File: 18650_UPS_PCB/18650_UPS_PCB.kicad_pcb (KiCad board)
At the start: 4 copper layers, 90 x 62 mm, 68 parts, among them J1 USB_B_Micro, J10 Conn_02x06_Odd_Even, J11 Conn_02x07_Odd_Even, J6 Conn_02x01, J9 Conn_02x04_Odd_Even, SW1 ENABLE, SW2 5_Way_Tactile, SW3 PWR MODE, SW5 ENABLE, U1 STLINK-V3MINI, U10 STLINK-V3MINI, U2 R5478, U3 STC4054, U4 FS8205A, U5 TPS63000, U6 TPS63000, U7 SSD1306_128_32, U8 INA219AxD, U9 STM32F030F4Px

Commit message: first routing done
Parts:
- removed JP3: A0_SEL, Jumper:SolderJumper-3_P1.3mm_Open_RoundedPad1.0x1.5mm
- removed JP4: A1_SEL, Jumper:SolderJumper-3_P1.3mm_Open_RoundedPad1.0x1.5mm
- removed R14, R15: 3.3 kOhm, Resistor_SMD:R_0603_1608Metric
- removed SW2: 5_Way_Tactile, CUSTOM_FOOTPRINTS:5_Way_Tactical
- added SW4: ALPSALPINE_SKRHADE011, CUSTOM_FOOTPRINTS:SKRHADE011, F.Cu at (154.5, 90.1)
- BT1: moved to B.Cu
- U7: footprint Connector_PinSocket_2.54mm:PinSocket_1x04_P2.54mm_Vertical -> Connector_PinHeader_2.54mm:PinHeader_1x04_P2.54mm_Vertical_SMD_Pin1Left
- moved J11 110.2 mm to (194.4, 79.2), turned to 270 degrees
- moved U1 101.3 mm to (177.1, 99.5)
- moved JP5 97.0 mm to (187.7, 100.7), turned to 270 degrees
- moved R12 92.6 mm to (188.1, 97.1), turned to 90 degrees
- moved R13 91.4 mm to (185.9, 97.1), turned to 90 degrees
- moved U7 88.6 mm to (164.5, 89.0)
- moved C10 85.8 mm to (140.9, 78.5)
- moved C8 85.8 mm to (140.9, 76.5)
- moved R10 85.8 mm to (144.5, 78.5)
- moved C9 85.7 mm to (144.5, 76.5)
- moved C13 85.5 mm to (171.7, 85.2)
- moved C6 84.8 mm to (144.7, 92.3)
- moved R8 84.7 mm to (144.5, 81.5), turned to 0 degrees
- moved C18 84.6 mm to (171.7, 88.6)
- moved C19 84.5 mm to (171.7, 90.6)
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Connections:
- U8 pad 1: Net-(JP4-Pad2) -> GNDD
- U8 pad 2: Net-(JP3-Pad2) -> GNDD
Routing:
- net GNDD: track 0.00 -> 127.0 mm, vias 0 -> 11
- net -BATT: track 0.00 -> 124.3 mm, vias 0 -> 11
- net I2C1_SCL: track 0.06 -> 102.2 mm, vias 0 -> 5
- net I2C1_SDA: track 0.00 -> 81.9 mm, vias 0 -> 3
- net RSPI1_MOSI: track 0.00 -> 67.4 mm, vias 0 -> 2
- net RSPI1_SCLK: track 0.00 -> 62.1 mm, vias 0 -> 2
- net RSPI1_MISO: track 0.00 -> 61.8 mm, vias 0 -> 2
- net PB1: track 0.00 -> 56.0 mm, vias 0 -> 2
- net RSPI1_CE2: track 0.00 -> 53.9 mm, vias 0 -> 2
- net PA9: track 0.00 -> 53.6 mm, vias 0 -> 2
- net RSPI0_CE0: track 8.30 -> 51.8 mm, vias 0 -> 2
- net Shunt-: track 0.00 -> 40.9 mm, vias 0 -> 3
- net PA10: track 0.00 -> 39.3 mm, vias 0 -> 2
- net RSPI0_SCLK: track 7.90 -> 43.6 mm, vias 0 -> 2
- net RSPI0_MISO: track 6.71 -> 40.6 mm, vias 0 -> 2
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- added copper zone on B.Cu, net -BATT
- added copper zone on F.Cu, net -BATT
- added copper zone on In2.Cu, net -BATT
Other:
- board size 90 x 62 mm -> 90 x 30 mm

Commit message: layout almost done
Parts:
- removed J10: Conn_02x06_Odd_Even, Connector_PinSocket_2.54mm:PinSocket_2x06_P2.54mm_Vertical_SMD
- removed J11: Conn_02x07_Odd_Even, Connector_PinSocket_2.54mm:PinSocket_2x07_P2.54mm_Vertical_SMD
- removed J6: Conn_02x01, Connector_PinSocket_2.54mm:PinSocket_2x03_P2.54mm_Vertical_SMD
- removed J9: Conn_02x04_Odd_Even, Connector_PinSocket_2.54mm:PinSocket_2x04_P2.54mm_Vertical_SMD
- removed JP1, JP2: PWRSAVE, Jumper:SolderJumper-3_P1.3mm_Open_RoundedPad1.0x1.5mm
- removed JP5: Jumper_NO_Small, Jumper:SolderJumper-2_P1.3mm_Open_RoundedPad1.0x1.5mm
- removed SW3: PWR MODE, Button_Switch_THT:SW_CuK_OS102011MA1QN1_SPDT_Angled
- removed SW4: ALPSALPINE_SKRHADE011, CUSTOM_FOOTPRINTS:SKRHADE011
- removed SW5: ENABLE, Button_Switch_THT:SW_CuK_OS102011MA1QN1_SPDT_Angled
- removed U10: STLINK-V3MINI, Connector_PinHeader_1.27mm:PinHeader_2x07_P1.27mm_Vertical_SMD
- added J2: Conn_02x04_Odd_Even, Connector_PinSocket_2.54mm:PinSocket_2x04_P2.54mm_Vertical_SMD, F.Cu at (156.5, 78.9)
- added SW2: ALPSALPINE_SKRHADE011, CUSTOM_FOOTPRINTS:SKRHADE011, F.Cu at (199.6, 89.7)
- BT1: footprint CUSTOM_FOOTPRINTS:Keystone_1042 -> Battery:BatteryHolder_Keystone_1042_1x18650
- SW1: value ENABLE -> SW_SPDT; footprint Button_Switch_THT:SW_CuK_OS102011MA1QN1_SPDT_Angled -> CUSTOM_FOOTPRINTS:ALPS_SPEF210101
- U7: value SSD1306_128_32 -> INA219AxD; footprint Connector_PinHeader_2.54mm:PinHeader_1x04_P2.54mm_Vertical_SMD_Pin1Left -> Package_SO:SOIC-8_3.9x4.9mm_P1.27mm
- U8: value INA219AxD -> SSD1306_128_32; footprint Package_SO:SOIC-8_3.9x4.9mm_P1.27mm -> Connector_PinHeader_2.54mm:PinHeader_1x04_P2.54mm_Vertical_SMD_Pin1Left
- moved U4 83.6 mm to (206.5, 84.3), turned to 0 degrees
- moved R2 81.9 mm to (126.6, 87.1), turned to 0 degrees
- moved U3 76.5 mm to (125.8, 83.1), turned to 0 degrees
- moved D1 76.1 mm to (129.1, 78.4), turned to 90 degrees
- moved U2 75.3 mm to (201.9, 79.2)
- moved R4 72.6 mm to (198.8, 79.4), turned to 90 degrees
- moved C2 72.3 mm to (198.8, 75.4)
- moved R1 72.1 mm to (202.3, 75.4)
- moved R3 70.6 mm to (132.3, 76.9), turned to 0 degrees
- moved R5 69.3 mm to (132.4, 80.2)
- moved C3 68.9 mm to (131.5, 83.1), turned to 270 degrees
- moved C1 67.0 mm to (133.5, 83.1), turned to 270 degrees
- moved J1 59.5 mm to (145.3, 76.7), turned to 180 degrees
- moved C12 57.4 mm to (137.8, 93.9), turned to 90 degrees
- moved C8 44.2 mm to (185.1, 76.5), turned to 90 degrees
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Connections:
- BT1 pad 1: Shunt+ -> Net-(BT1-Pad1)
- C13 pad 1: GNDD -> +3V3
- C13 pad 2: NRST -> GNDD
- C14 pad 1: +3V3 -> GNDD
- C14 pad 2: GNDD -> NRST
- C15 pad 2: MCU_PWR -> +3V3
- C16 pad 2: MCU_PWR -> +3V3
- C17 pad 2: MCU_PWR -> +3V3
- C18 pad 1: MCU_PWR -> +3V3
- C19 pad 1: MCU_PWR -> +3V3
- R12 pad 1: Net-(JP5-Pad1) -> +3V3
- R13 pad 1: Net-(JP5-Pad1) -> +3V3
- SW1 pad 1: Net-(C6-Pad2) -> Net-(SW1-Pad1)
- SW1 pad 2: Net-(JP1-Pad3) -> Net-(BT1-Pad1)
- SW1 pad 3: GNDD -> Shunt+
- U1 pad 3: MCU_PWR -> +3V3
- U5 pad 6: Net-(JP1-Pad3) -> Net-(C6-Pad2)
- U5 pad 7: Net-(JP1-Pad2) -> PA4
- U6 pad 6: Net-(JP2-Pad3) -> Net-(C7-Pad2)
- U6 pad 7: Net-(JP2-Pad2) -> PA5
- U7 pad 2: MCU_PWR -> GNDD
- U7 pad 3: I2C1_SCL -> I2C1_SDA
- U7 pad 4: I2C1_SDA -> I2C1_SCL
- U8 pad 2: GNDD -> +3V3
- U8 pad 3: I2C1_SDA -> I2C1_SCL
- U8 pad 4: I2C1_SCL -> I2C1_SDA
- U9 pad 10: RSPI0_CE0 -> PA4
- U9 pad 11: RSPI0_SCLK -> PA5
- U9 pad 12: RSPI0_MISO -> Net-(U9-Pad12)
- U9 pad 13: RSPI0_MOSI -> Net-(U9-Pad13)
- U9 pad 16: MCU_PWR -> +3V3
- U9 pad 5: MCU_PWR -> +3V3
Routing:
- net -BATT: track 124.3 -> 52.2 mm, vias 11 -> 4
- net GNDD: track 127.0 -> 58.2 mm, vias 11 -> 14
- net RSPI1_MOSI: track 67.4 -> 0.00 mm, vias 2 -> 0
- net RSPI1_SCLK: track 62.1 -> 0.00 mm, vias 2 -> 0
- net RSPI1_MISO: track 61.8 -> 0.00 mm, vias 2 -> 0
- net RSPI1_CE2: track 53.9 -> 0.00 mm, vias 2 -> 0
- net RSPI0_CE0: track 51.8 -> 0.00 mm, vias 2 -> 0
- net I2C1_SCL: track 102.2 -> 56.3 mm, vias 5 -> 3
- net RSPI0_SCLK: track 43.6 -> 0.00 mm, vias 2 -> 0
- net RSPI0_MISO: track 40.6 -> 0.00 mm, vias 2 -> 0
- net RSPI0_MOSI: track 38.8 -> 0.00 mm, vias 2 -> 0
- net PB1: track 56.0 -> 17.6 mm
- net PA9: track 53.6 -> 19.6 mm, vias 2 -> 0
- net RSWCLK: track 32.6 -> 0.00 mm
- net Net-(BT1-Pad1): track 0.00 -> 30.3 mm, vias 0 -> 6
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- added copper zone on F.Cu, net GNDD
- added copper zone on B.Cu, net Net-(BT1-Pad1)
- added copper zone on F.Cu, net Net-(BT1-Pad1)
- removed copper zone on In2.Cu, net -BATT
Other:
- board size 90 x 30 mm -> 90 x 22 mm

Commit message: routing done
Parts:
- moved R8 2.57 mm to (182.2, 84.5)
- moved R9 1.78 mm to (170.7, 84.5)
- moved U5 0.65 mm to (179.5, 81.0)
- moved C7 0.51 mm to (164.8, 84.5)
- moved C6 0.44 mm to (176.3, 84.5)
- moved C14 0.41 mm to (172.3, 88.6)
- moved L1 0.39 mm to (179.4, 76.5)
- moved R10 0.36 mm to (183.0, 81.5)
- moved C10 0.30 mm to (183.0, 76.5)
- moved U6 0.30 mm to (167.6, 81.0)
- moved R6 0.28 mm to (175.5, 81.5)
- moved R7 0.28 mm to (164.0, 81.5)
- moved C11 0.22 mm to (173.5, 81.5)
- moved R11 0.22 mm to (171.5, 81.5)
- moved C4 0.20 mm to (175.5, 76.5)
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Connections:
- U6 pad 6: Net-(C7-Pad2) -> PA6
- U9 pad 12: Net-(U9-Pad12) -> PA6
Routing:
- net +3V3: track 45.1 -> 154.5 mm, vias 7 -> 10
- net Shunt-: track 17.8 -> 117.5 mm, vias 1 -> 9
- net -BATT: track 52.2 -> 126.4 mm, vias 4 -> 7
- net +5V: track 4.45 -> 37.4 mm, vias 1 -> 4
- net PA6: track 0.00 -> 27.5 mm, vias 0 -> 2
- net PA5: track 1.73 -> 26.2 mm, vias 1 -> 2
- net GNDD: track 58.2 -> 81.6 mm, vias 14 -> 20
- net PA4: track 2.27 -> 18.9 mm, vias 1 -> 2
- net Net-(C6-Pad2): track 0.00 -> 11.6 mm
- net Net-(C7-Pad2): track 0.00 -> 9.30 mm, vias 0 -> 2
- net Net-(C11-Pad2): track 0.00 -> 7.16 mm
- net Net-(C9-Pad2): track 0.00 -> 6.88 mm
- net USART1_RX: track 30.7 -> 26.2 mm
- net Net-(L1-Pad2): track 0.00 -> 3.76 mm
- net PA1: track 31.9 -> 28.3 mm
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- added copper zone on B.Cu, net +3V3
- added copper zone on F.Cu, net +3V3
- added copper zone on In2.Cu, net +3V3
- added copper zone on F.Cu, net +5V
- added copper zone on In2.Cu, net +5V
- added copper zone on In2.Cu, net -BATT
- added copper zone on F.Cu, net Shunt-
- added copper zone on In2.Cu, net Shunt-

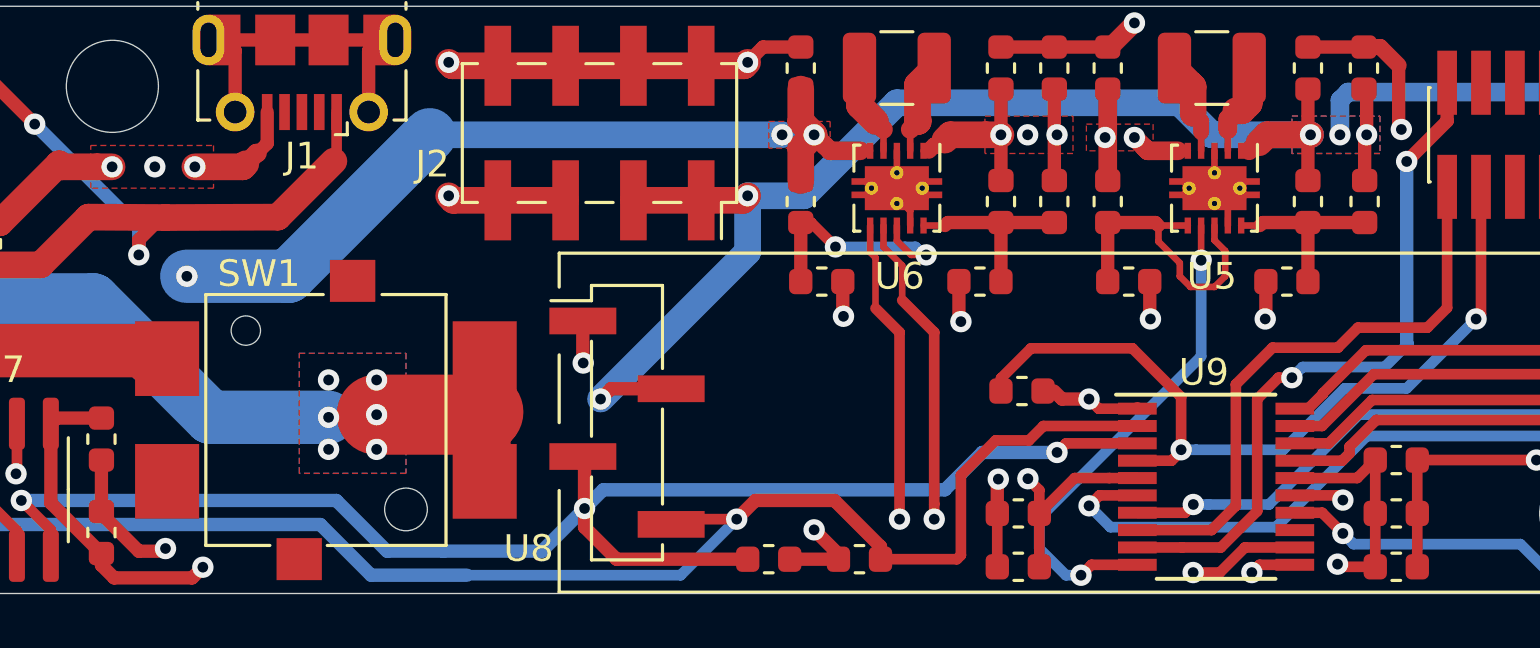
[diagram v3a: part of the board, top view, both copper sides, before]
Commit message: changed resistor values tps63000
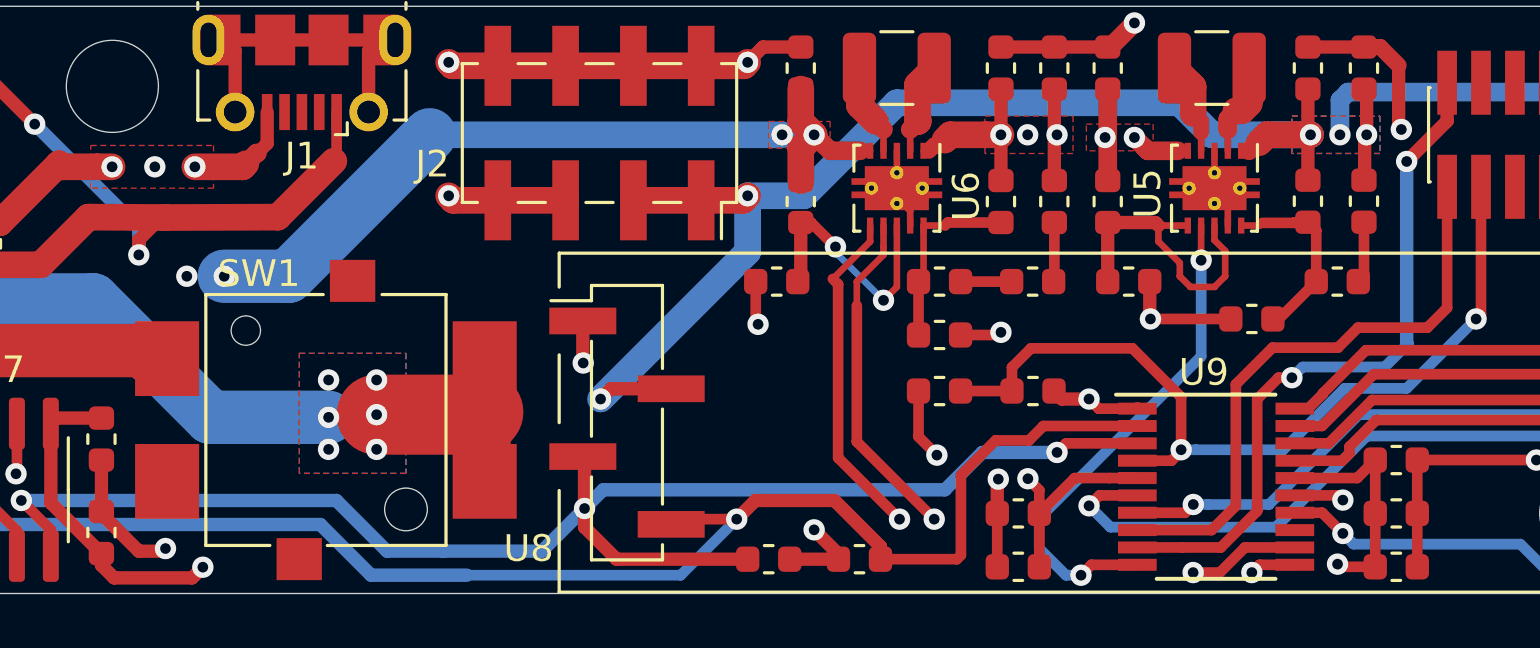
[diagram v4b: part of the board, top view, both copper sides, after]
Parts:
- added R14: 680 kOhm, Resistor_SMD:R_0603_1608Metric, F.Cu at (172.7, 84.5)
- added R15: 100 kOhm, Resistor_SMD:R_0603_1608Metric, F.Cu at (185.1, 81.5)
- added R16: 120 kOhm, Resistor_SMD:R_0603_1608Metric, F.Cu at (173.5, 81.5)
- added R17: 10 kOhm, Resistor_SMD:R_0603_1608Metric, F.Cu at (169.2, 88.6)
- R10: value 1.1 MOhm -> 1 MOhm
- R11: value 1.8 MOhm -> 1 MOhm
- moved R11 3.78 mm to (169.2, 84.5), turned to 180 degrees
- moved R10 3.20 mm to (184.1, 84.5), turned to 180 degrees
- moved R9 2.51 mm to (169.2, 86.5), turned to 180 degrees
- moved C9 2.13 mm to (183.0, 81.5)
- moved C11 2.00 mm to (171.5, 81.5)
- moved R8 1.92 mm to (180.9, 85.9)
- moved C7 1.69 mm to (163.1, 84.5), turned to 0 degrees
- moved C14 0.41 mm to (172.7, 88.6)
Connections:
- R10 pad 1: +3V3 -> Net-(R10-Pad1)
- R11 pad 1: +5V -> Net-(R11-Pad1)
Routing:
- net +3V3: track 154.5 -> 157.2 mm, vias 10 -> 11
- net Net-(R10-Pad1): track 0.00 -> 2.31 mm
- net Net-(R14-Pad1): track 0.00 -> 2.22 mm
- net GNDD: track 81.6 -> 83.6 mm, vias 20 -> 19
- net Net-(R11-Pad1): track 0.00 -> 1.91 mm
- net NRST: track 30.4 -> 32.1 mm
- net PA6: track 27.5 -> 28.6 mm
- net PA5: track 26.2 -> 27.1 mm
- net -BATT: track 126.4 -> 125.6 mm
- net Shunt-: vias 9 -> 10

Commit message: ordered
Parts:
- U3: footprint Package_TO_SOT_SMD:TSOT-23-5_HandSoldering -> Package_TO_SOT_SMD:TSOT-23-5
- turned U8 to 180 degrees
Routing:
- net I2C1_SDA: track 55.9 -> 66.1 mm
- net I2C1_SCL: track 56.3 -> 60.3 mm
- net GNDD: track 83.6 -> 87.1 mm, vias 19 -> 18
- net USART1_RX: track 26.2 -> 24.3 mm
- net NRST: track 32.1 -> 30.8 mm
- added copper zone on B.Cu, net Shunt-
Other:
- board text added: "GGGG 5533"
